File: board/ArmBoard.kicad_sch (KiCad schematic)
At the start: 0 parts

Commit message: Changing CRX and CTX Round 2 :((
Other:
- sheet CAN ports: added CANRX3, CANTX3; removed CANRX7, CANTX7
- sheet MCU ports: added CANRX3, CANTX3; removed CANRX7, CANTX7
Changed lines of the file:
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@@
 			)
 		)
-		(pin "CANTX7" output
+		(pin "CANTX3" output
 			(at 48.26 157.48 0)
 			(effects
@@
 			)
 		)
-		(pin "CANRX7" input
+		(pin "CANRX3" input
 			(at 48.26 154.94 0)
 			(effects
@@
 			)
 		)
-		(pin "CANTX7" input
+		(pin "CANTX3" input
 			(at 48.26 105.41 0)
 			(effects
@@
 			)
 		)
-		(pin "CANRX7" output
+		(pin "CANRX3" output
 			(at 48.26 102.87 0)
 			(effects

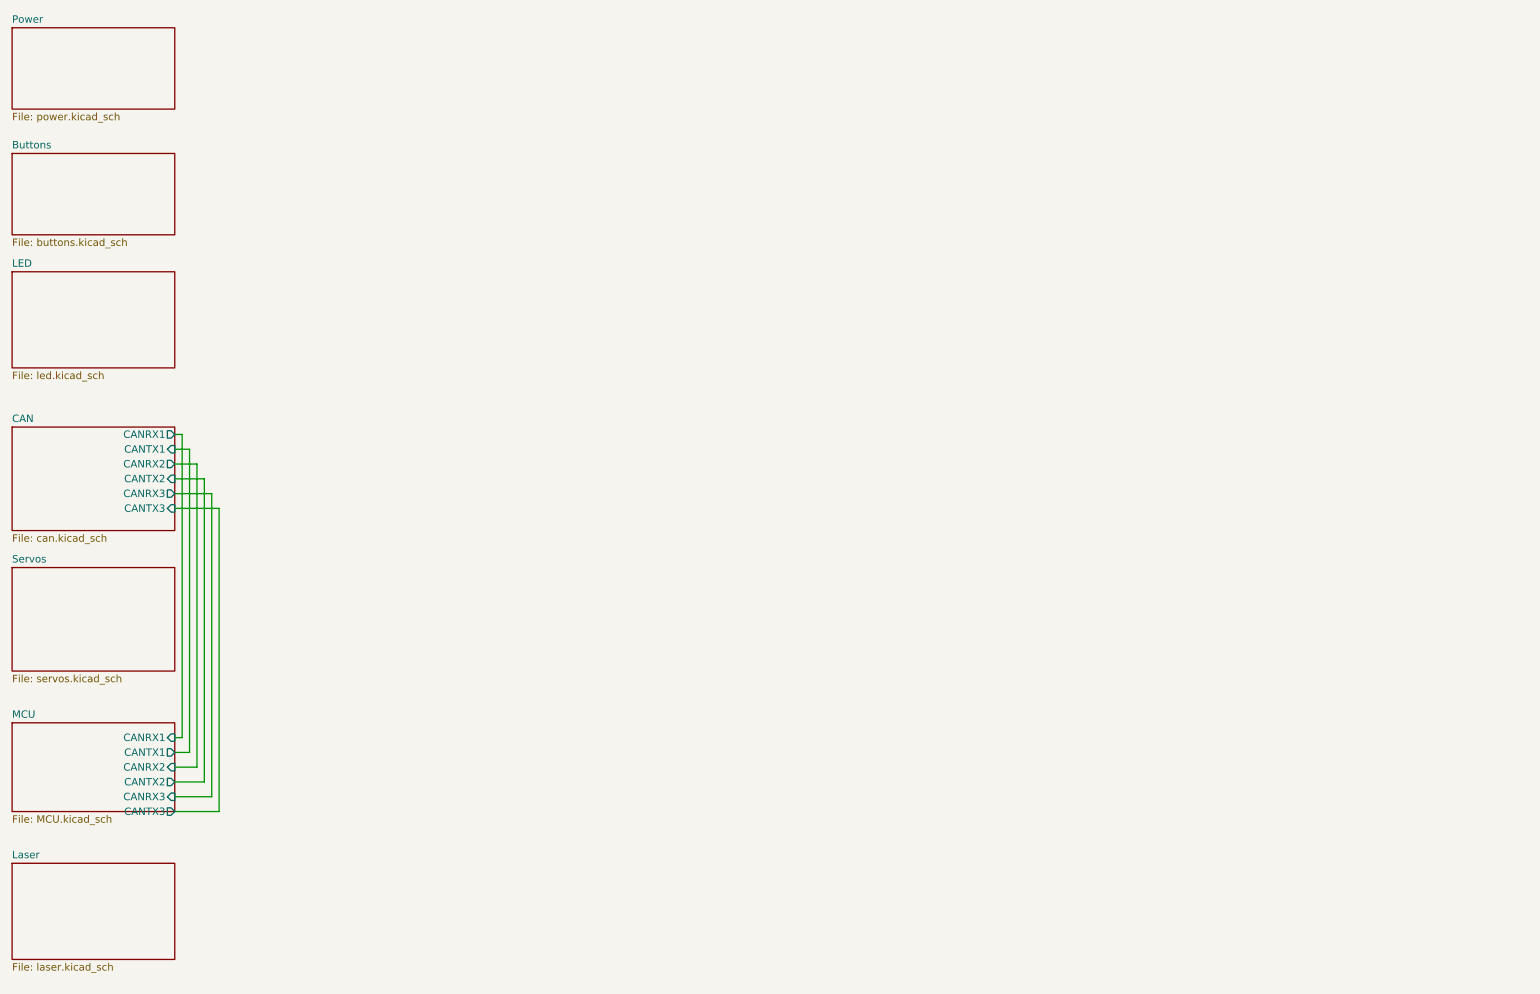
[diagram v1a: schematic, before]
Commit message: rearranged root
made root more organized and workable
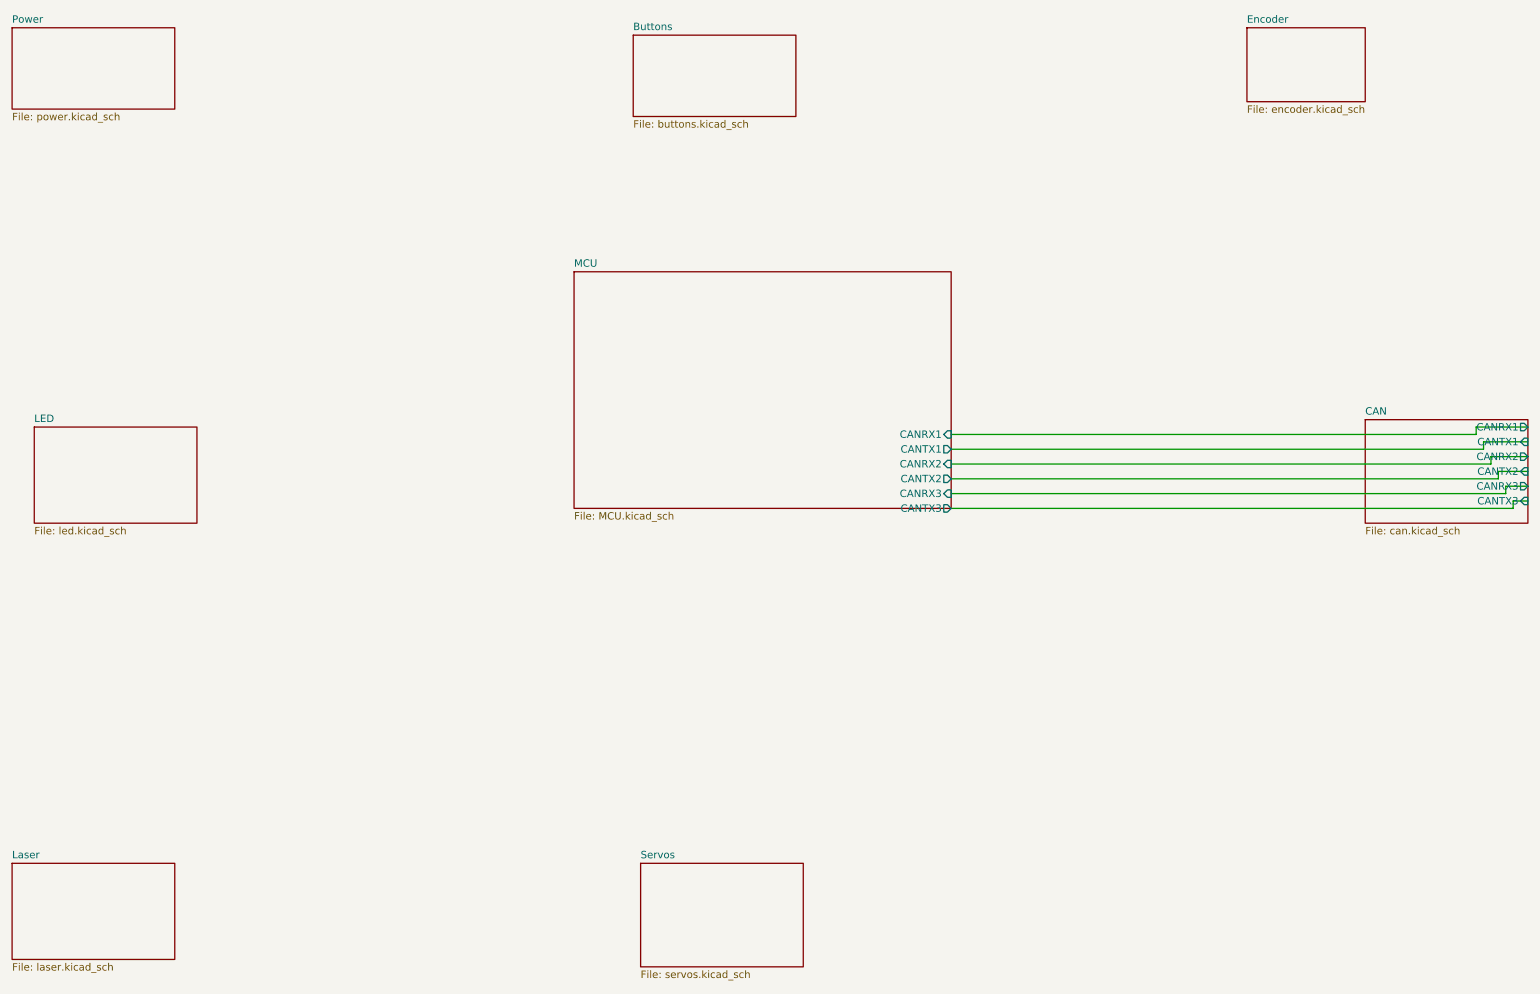
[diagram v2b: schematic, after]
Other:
- added sheet Encoder (encoder.kicad_sch)

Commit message: Added root pins
Root beer
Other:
- sheet Buttons ports: added B_1, B_2, B_3, B_4, B_5, B_6, B_7, B_8, Dirc_swt, Laser, Lin_serv, Serv_1, Serv_2, Serv_3, Serv_4; removed none
- sheet Servos ports: added Serv_pwm_1, Serv_pwm_2, Serv_pwm_3, Serv_pwm_4, Serv_pwm_lin; removed none
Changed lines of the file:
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@@
+			)
+		)
+		(pin "Serv_pwm_1" input
+			(at 151.13 166.37 90)
+			(effects
+				(font
+					(size 1.27 1.27)
+				)
+				(justify right)
+			)
+		)
+		(pin "Serv_pwm_2" input
+			(at 147.32 166.37 90)
+			(effects
+				(font
+					(size 1.27 1.27)
+				)
+				(justify right)
+			)
+		)
+		(pin "Serv_pwm_3" input
+			(at 142.24 166.37 90)
+			(effects
+				(font
+					(size 1.27 1.27)
+				)
+				(justify right)
+			)
+		)
+		(pin "Serv_pwm_4" input
+			(at 135.89 166.37 90)
+			(effects
+				(font
+					(size 1.27 1.27)
+				)
+				(justify right)
+			)
+		)
+		(pin "Serv_pwm_lin" input
+			(at 130.81 166.37 90)
+			(effects
+				(font
+					(size 1.27 1.27)
+				)
+				(justify right)
 			)
 		)
@@
 			)
 		)
+		(pin "B_1" output
+			(at 154.94 26.67 0)
+			(effects
+				(font
+					(size 1.27 1.27)
+				)
+				(justify right)
+			)
+		)
+		(pin "B_2" output
+			(at 154.94 29.21 0)
+			(effects
+				(font
+					(size 1.27 1.27)
+				)
+				(justify right)
+			)
+		)
+		(pin "B_3" output
+			(at 154.94 31.75 0)
+			(effects
+				(font
+					(size 1.27 1.27)
+				)
+				(justify right)
+			)
+		)
+		(pin "B_4" output
+			(at 154.94 34.29 0)
+			(effects
+				(font
+					(size 1.27 1.27)
+				)
+				(justify right)
+			)
+		)
+		(pin "B_5" output
+			(at 154.94 36.83 0)
+			(effects
+				(font
+					(size 1.27 1.27)
+				)
+				(justify right)
+			)
+		)
+		(pin "B_6" output
+			(at 129.54 38.1 270)
+			(effects
+				(font
+					(size 1.27 1.27)
+				)
+				(justify left)
+			)
+		)
+		(pin "B_7" output
+			(at 132.08 38.1 270)
+			(effects
+				(font
+					(size 1.27 1.27)
+				)
+				(justify left)
+			)
+		)
+		(pin "B_8" output
+			(at 134.62 38.1 270)
+			(effects
+				(font
+					(size 1.27 1.27)
+				)
+				(justify left)
+			)
+		)
+		(pin "Dirc_swt" output
+			(at 137.16 38.1 270)
+			(effects
+				(font
+					(size 1.27 1.27)
+				)
+				(justify left)
+			)
+		)
+		(pin "Laser" output
+			(at 139.7 38.1 270)
+			(effects
+				(font
+					(size 1.27 1.27)
+				)
+				(justify left)
+			)
+		)
+		(pin "Lin_serv" output
+			(at 142.24 38.1 270)
+			(effects
+				(font
+					(size 1.27 1.27)
+				)
+				(justify left)
+			)
+		)
+		(pin "Serv_1" output
+			(at 144.78 38.1 270)
+			(effects
+				(font
+					(size 1.27 1.27)
+				)
+				(justify left)
+			)
+		)
+		(pin "Serv_2" output
+			(at 147.32 38.1 270)
+			(effects
+				(font
+					(size 1.27 1.27)
+				)
+				(justify left)
+			)
+		)
+		(pin "Serv_3" output
+			(at 127 27.94 180)
+			(effects
+				(font
+					(size 1.27 1.27)
+				)
+				(justify left)
+			)
+		)
+		(pin "Serv_4" output
+			(at 127 30.48 180)
+			(effects
+				(font
+					(size 1.27 1.27)
+				)
+				(justify left)
+			)
+		)

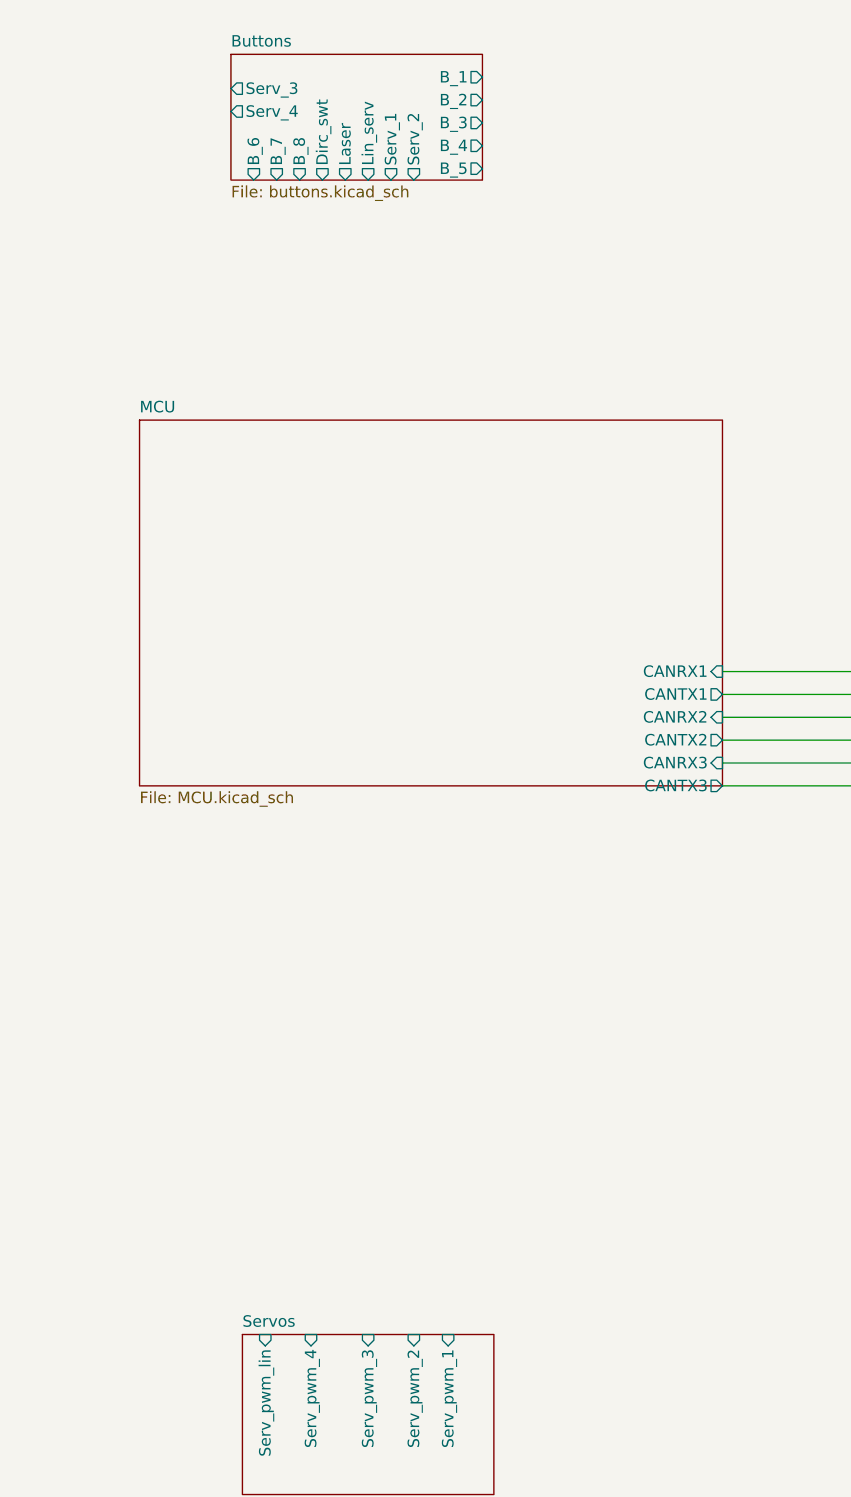
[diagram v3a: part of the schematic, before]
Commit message: Wires ran
Wires run between pins
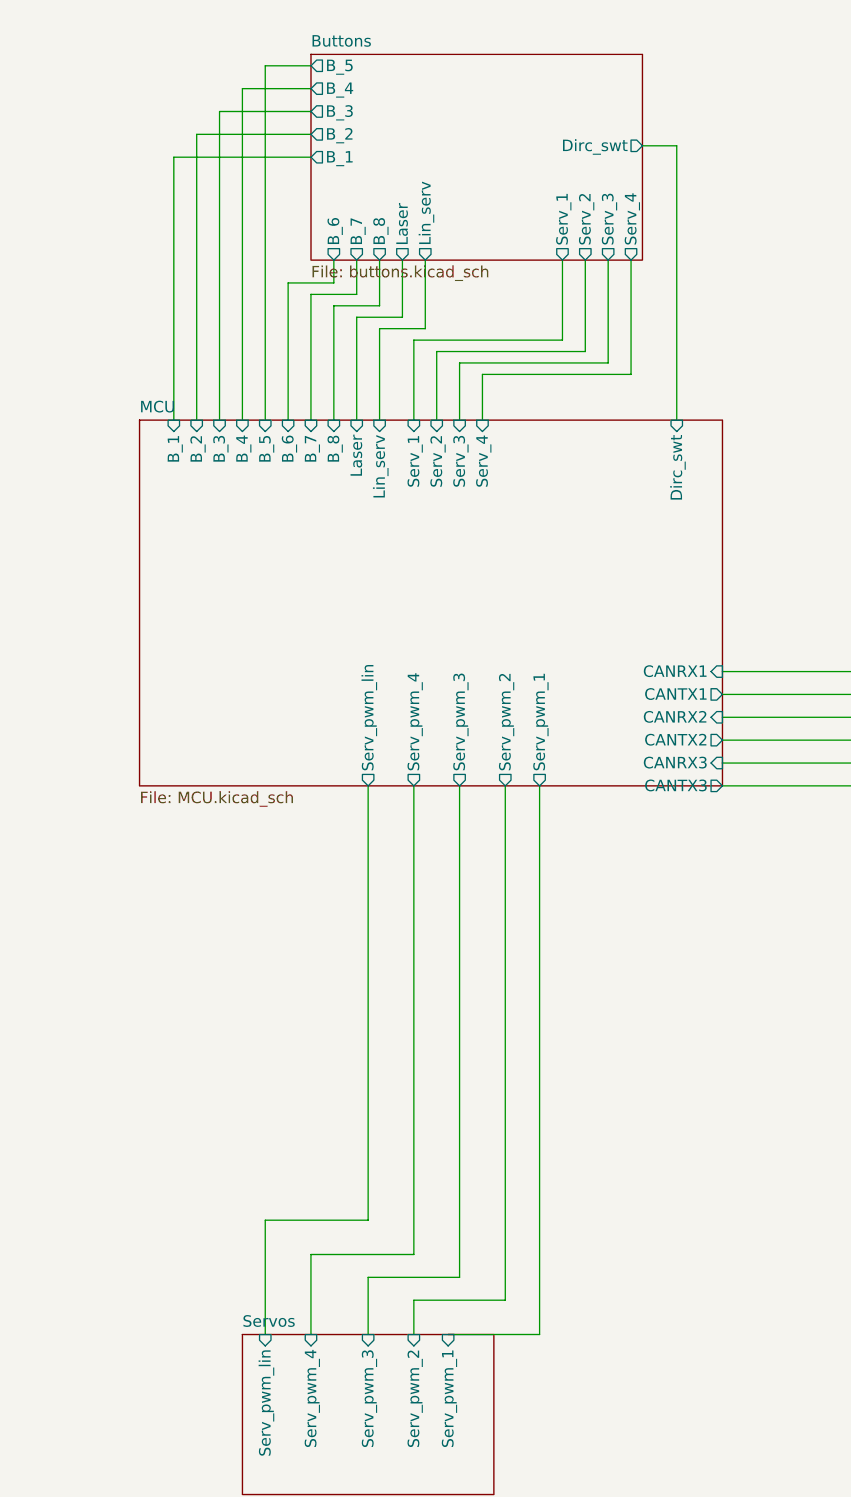
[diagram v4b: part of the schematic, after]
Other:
- sheet MCU ports: added B_1, B_2, B_3, B_4, B_5, B_6, B_7, B_8, Dirc_swt, Laser, Lin_serv, Serv_1, Serv_2, Serv_3, Serv_4, Serv_pwm_1, Serv_pwm_2, Serv_pwm_3, Serv_pwm_4, Serv_pwm_lin; removed none

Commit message: Final 1
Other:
- removed sheet Encoder
- removed sheet LED
- sheet Laser ports: added LAS; removed none
- sheet MCU ports: added LAS; removed none

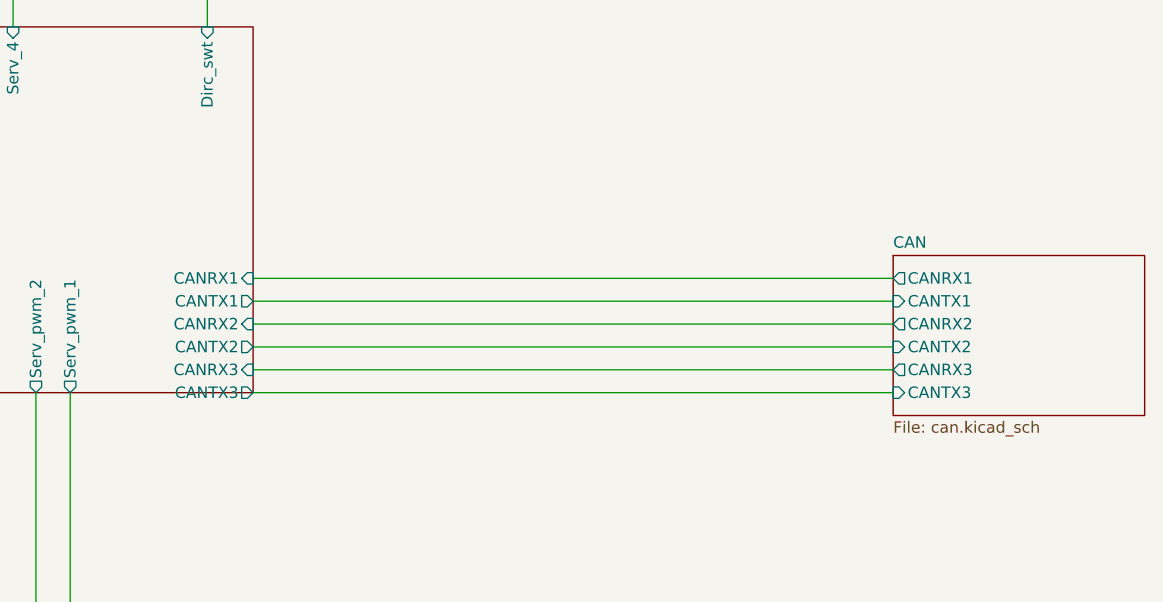
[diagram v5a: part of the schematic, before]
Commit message: Schematic review changes
Updated molex connectors, can ics, buttons are no longer pull ups, and some appearence changes.
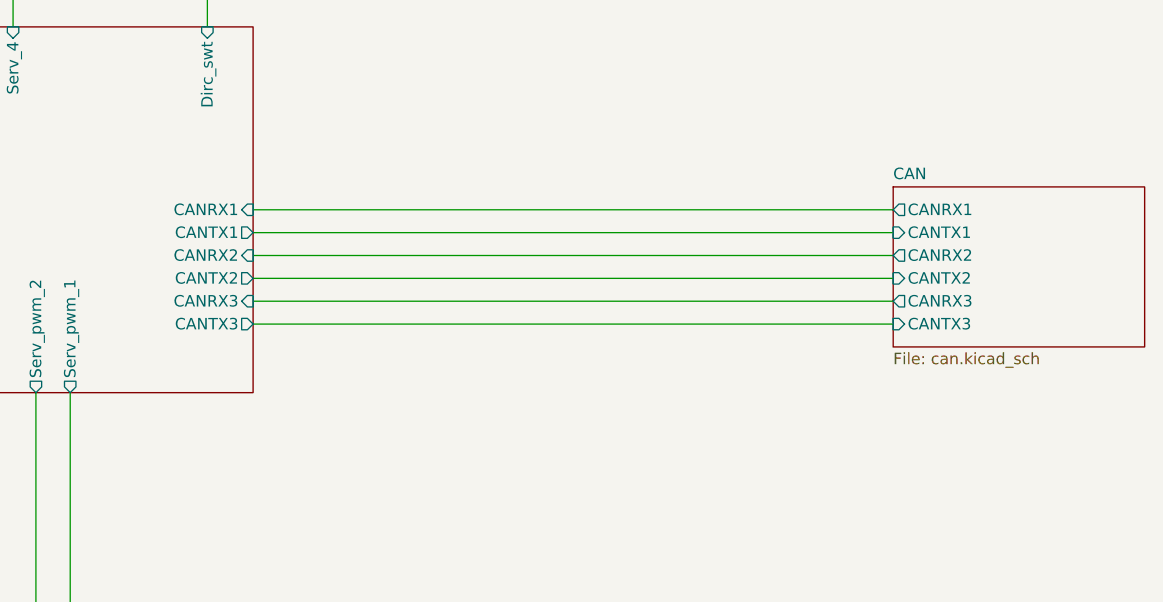
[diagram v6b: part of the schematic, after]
